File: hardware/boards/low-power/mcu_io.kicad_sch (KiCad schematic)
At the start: 8 parts, among them SW2 SW_SPST, U12 TMUX1309BQBR, U17 TCA9539RTWR

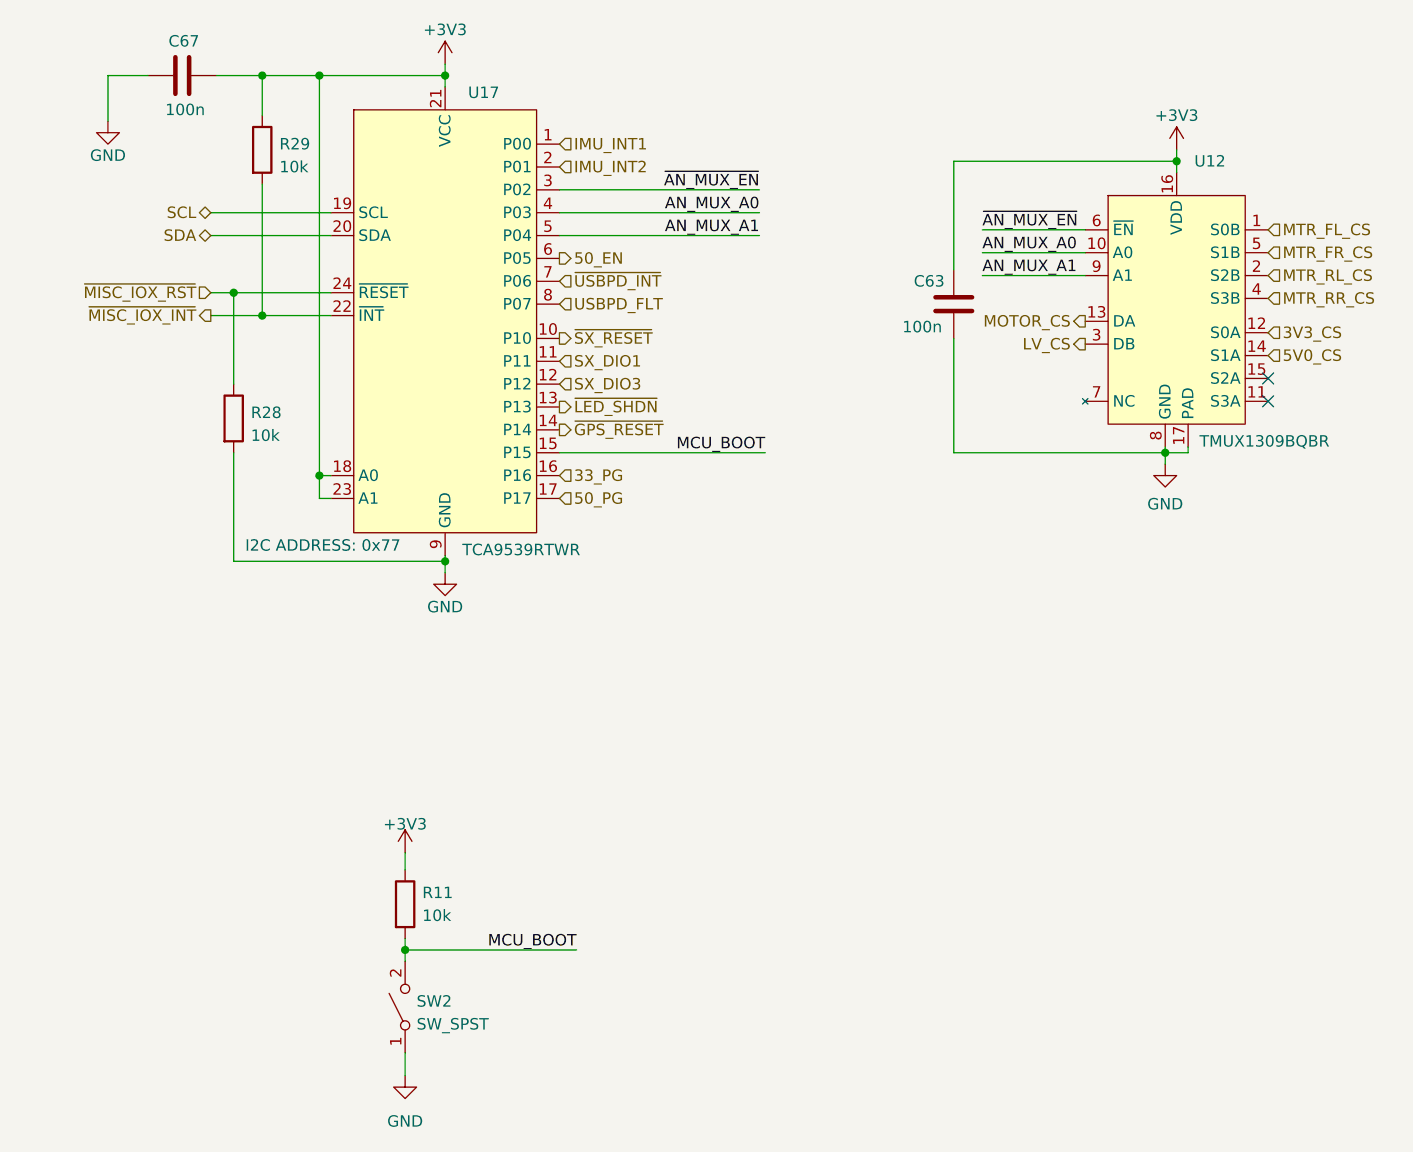
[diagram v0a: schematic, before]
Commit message: Add footprints and models for LP board
Also completed rough layout for LP board to estimate board space usage.
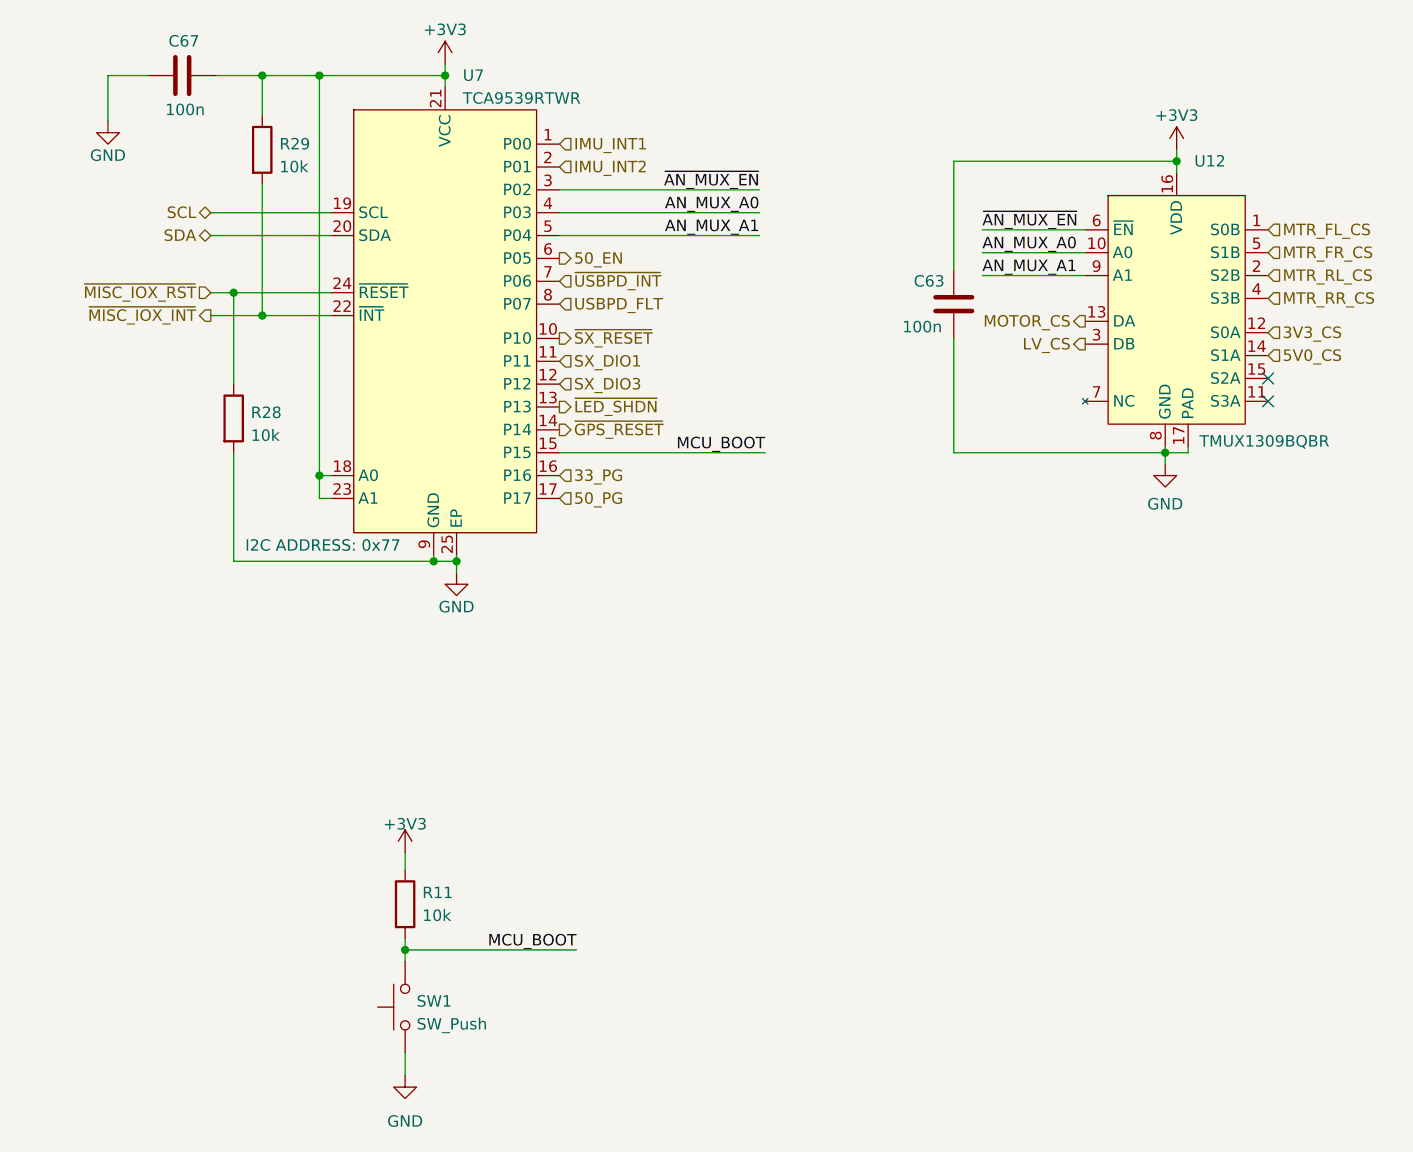
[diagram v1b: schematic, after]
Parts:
- removed SW2: SW_SPST, symbol Switch:SW_SPST
- removed U17: TCA9539RTWR, Package_DFN_QFN:WQFN-24-1EP_4x4mm_P0.5mm_EP2.45x2.45mm, symbol Capstone:TCA9539RTWR_
- added SW1: SW_Push, capstone:R-668048, symbol Switch:SW_Push
- added U7: TCA9539RTWR, Package_DFN_QFN:WQFN-24-1EP_4x4mm_P0.5mm_EP2.45x2.45mm, symbol Capstone:TCA9539RTWR_
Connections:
- net +3V3: now also U7.18 (A0), U7.21 (VCC), U7.23 (A1)
- net 33_PG: now also U7.16 (P16)
- net 50_EN: now also U7.6 (P05)
- net 50_PG: now also U7.17 (P17)
- net AN_MUX_A0: now also U7.4 (P03)
- net AN_MUX_A1: now also U7.5 (P04)
- net GND: now also SW1.1, U7.25 (EP), U7.9 (GND)
- net IMU_INT1: now also U7.1 (P00)
- net IMU_INT2: now also U7.2 (P01)
- net MCU_BOOT: now also SW1.2, U7.15 (P15)
- net SCL: now also U7.19 (SCL)
- net SDA: now also U7.20 (SDA)
- net SX_DIO1: now also U7.11 (P11)
- net SX_DIO3: now also U7.12 (P12)
- net USBPD_FLT: now also U7.8 (P07)
- net ~{AN_MUX_EN}: now also U7.3 (P02)
- net ~{GPS_RESET}: now also U7.14 (P14)
- net ~{LED_SHDN}: now also U7.13 (P13)
- net ~{MISC_IOX_INT}: now also U7.22 (~{INT})
- net ~{MISC_IOX_RST}: now also U7.24 (~{RESET})
- net ~{SX_RESET}: now also U7.10 (P10)
- net ~{USBPD_INT}: now also U7.7 (P06)

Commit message: Add initial changes after schematic review
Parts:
- renumbered R11 to R603, U7 to U601
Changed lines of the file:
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@@
         )
         (path "/71f6a5b4-1ac6-435b-9486-30b16ab86e62/1fffdcfb-a6c7-4a3c-aa2e-5ae87e2ce998"
-          (reference "U8") (unit 1)
+          (reference "U602") (unit 1)
         )
       )
@@
   )
   (symbol (lib_id "power:+3V3") (at 111.76 152.4 0) (unit 1)
-    (in_bom yes) (on_board yes) (dnp no) (fields_autoplaced)
-    (property "Reference" "#PWR041" (at 111.76 156.21 0)
-      (effects (font (size 1.27 1.27)) hide)
-    )
-    (property "Value" "+3V3" (at 111.76 149.225 0)
+    (in_bom yes) (on_board yes) (dnp no)
+    (property "Reference" "#PWR0602" (at 111.76 156.21 0)
+      (effects (font (size 1.27 1.27)) hide)
+    )
+    (property "Value" "+3V3" (at 111.76 148.59 0)
       (effects (font (size 1.27 1.27)))
     )
@@
       (project "low-power"
         (path "/71f6a5b4-1ac6-435b-9486-30b16ab86e62/1fffdcfb-a6c7-4a3c-aa2e-5ae87e2ce998"
-          (reference "#PWR041") (unit 1)
+          (reference "#PWR0602") (unit 1)
         )
       )
@@
         )
         (path "/71f6a5b4-1ac6-435b-9486-30b16ab86e62/1fffdcfb-a6c7-4a3c-aa2e-5ae87e2ce998"
-          (reference "#PWR044") (unit 1)
+          (reference "#PWR0605") (unit 1)
         )
       )
@@
         )
         (path "/71f6a5b4-1ac6-435b-9486-30b16ab86e62/1fffdcfb-a6c7-4a3c-aa2e-5ae87e2ce998"
-          (reference "#PWR040") (unit 1)
+          (reference "#PWR0601") (unit 1)
         )
       )
@@
         )
         (path "/71f6a5b4-1ac6-435b-9486-30b16ab86e62/1fffdcfb-a6c7-4a3c-aa2e-5ae87e2ce998"
-          (reference "C46") (unit 1)
+          (reference "C601") (unit 1)
         )
       )
@@
   (symbol (lib_id "Device:R") (at 111.76 158.115 0) (unit 1)
     (in_bom yes) (on_board yes) (dnp no)
-    (property "Reference" "R11" (at 113.665 156.845 0)
+    (property "Reference" "R603" (at 113.665 156.845 0)
       (effects (font (size 1.27 1.27)) (justify left))
     )
@@
       (project "low-power"
         (path "/71f6a5b4-1ac6-435b-9486-30b16ab86e62/1fffdcfb-a6c7-4a3c-aa2e-5ae87e2ce998"
-          (reference "R11") (unit 1)
+          (reference "R603") (unit 1)
         )
       )
@@
         )
         (path "/71f6a5b4-1ac6-435b-9486-30b16ab86e62/1fffdcfb-a6c7-4a3c-aa2e-5ae87e2ce998"
-          (reference "#PWR043") (unit 1)
+          (reference "#PWR0604") (unit 1)
         )
       )
@@
         )
         (path "/71f6a5b4-1ac6-435b-9486-30b16ab86e62/1fffdcfb-a6c7-4a3c-aa2e-5ae87e2ce998"
-          (reference "C47") (unit 1)
+          (reference "C602") (unit 1)
         )
       )
@@
   (symbol (lib_id "power:GND") (at 111.76 177.165 0) (unit 1)
     (in_bom yes) (on_board yes) (dnp no) (fields_autoplaced)
-    (property "Reference" "#PWR042" (at 111.76 183.515 0)
+    (property "Reference" "#PWR0603" (at 111.76 183.515 0)
       (effects (font (size 1.27 1.27)) hide)
     )
@@
       (project "low-power"
         (path "/71f6a5b4-1ac6-435b-9486-30b16ab86e62/1fffdcfb-a6c7-4a3c-aa2e-5ae87e2ce998"
-          (reference "#PWR042") (unit 1)
+          (reference "#PWR0603") (unit 1)
         )
       )
@@
         )
         (path "/71f6a5b4-1ac6-435b-9486-30b16ab86e62/1fffdcfb-a6c7-4a3c-aa2e-5ae87e2ce998"
-          (reference "R9") (unit 1)
+          (reference "R601") (unit 1)
         )
       )
@@
         )
         (path "/71f6a5b4-1ac6-435b-9486-30b16ab86e62/1fffdcfb-a6c7-4a3c-aa2e-5ae87e2ce998"
-          (reference "#PWR046") (unit 1)
+          (reference "#PWR0607") (unit 1)
         )
       )
@@
         )
         (path "/71f6a5b4-1ac6-435b-9486-30b16ab86e62/1fffdcfb-a6c7-4a3c-aa2e-5ae87e2ce998"
-          (reference "#PWR045") (unit 1)
+          (reference "#PWR0606") (unit 1)
         )
       )
@@
         )
         (path "/71f6a5b4-1ac6-435b-9486-30b16ab86e62/1fffdcfb-a6c7-4a3c-aa2e-5ae87e2ce998"
-          (reference "R10") (unit 1)
+          (reference "R602") (unit 1)
         )
       )
@@
   (symbol (lib_id "Capstone:TCA9539RTWR_") (at 116.205 92.71 0) (unit 1)
     (in_bom yes) (on_board yes) (dnp no) (fields_autoplaced)
-    (property "Reference" "U7" (at 118.1609 66.04 0)
+    (property "Reference" "U601" (at 118.1609 66.04 0)
       (effects (font (size 1.27 1.27)) (justify left))
     )
@@
       (project "low-power"
         (path "/71f6a5b4-1ac6-435b-9486-30b16ab86e62/1fffdcfb-a6c7-4a3c-aa2e-5ae87e2ce998"
-          (reference "U7") (unit 1)
+          (reference "U601") (unit 1)
         )
       )
@@
         )
         (path "/71f6a5b4-1ac6-435b-9486-30b16ab86e62/1fffdcfb-a6c7-4a3c-aa2e-5ae87e2ce998"
-          (reference "SW2") (unit 1)
-        )
-      )
+          (reference "SW601") (unit 1)
+        )
+      )
